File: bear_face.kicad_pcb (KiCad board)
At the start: 2 copper layers, 301.7 x 112.6 mm, 194 parts, among them J1 USB_B_Micro, J2 Conn_02x03_Odd_Even, Q1 2N7002, SW1 SW_Push, U1 ATmega32U4-AU, U2 SRV05-4, Y1 16MHz

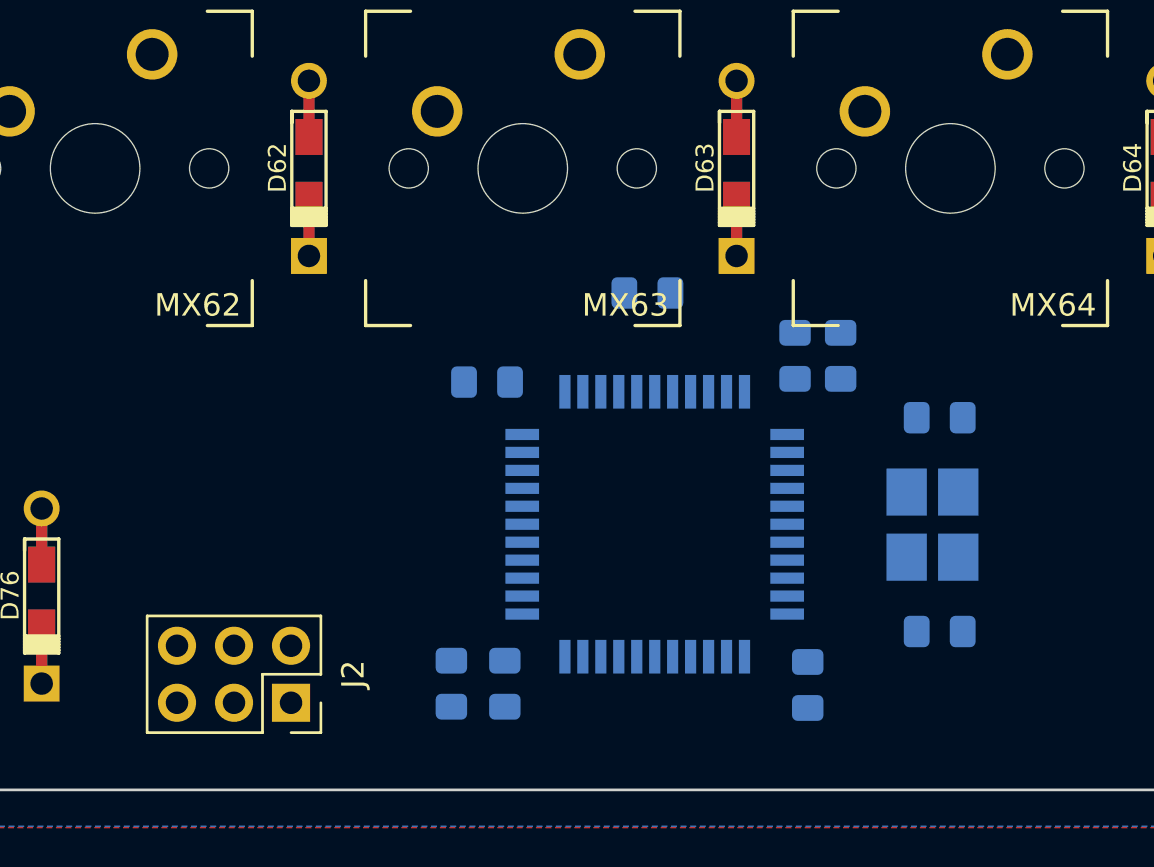
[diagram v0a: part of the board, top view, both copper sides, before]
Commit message: MCU components routed
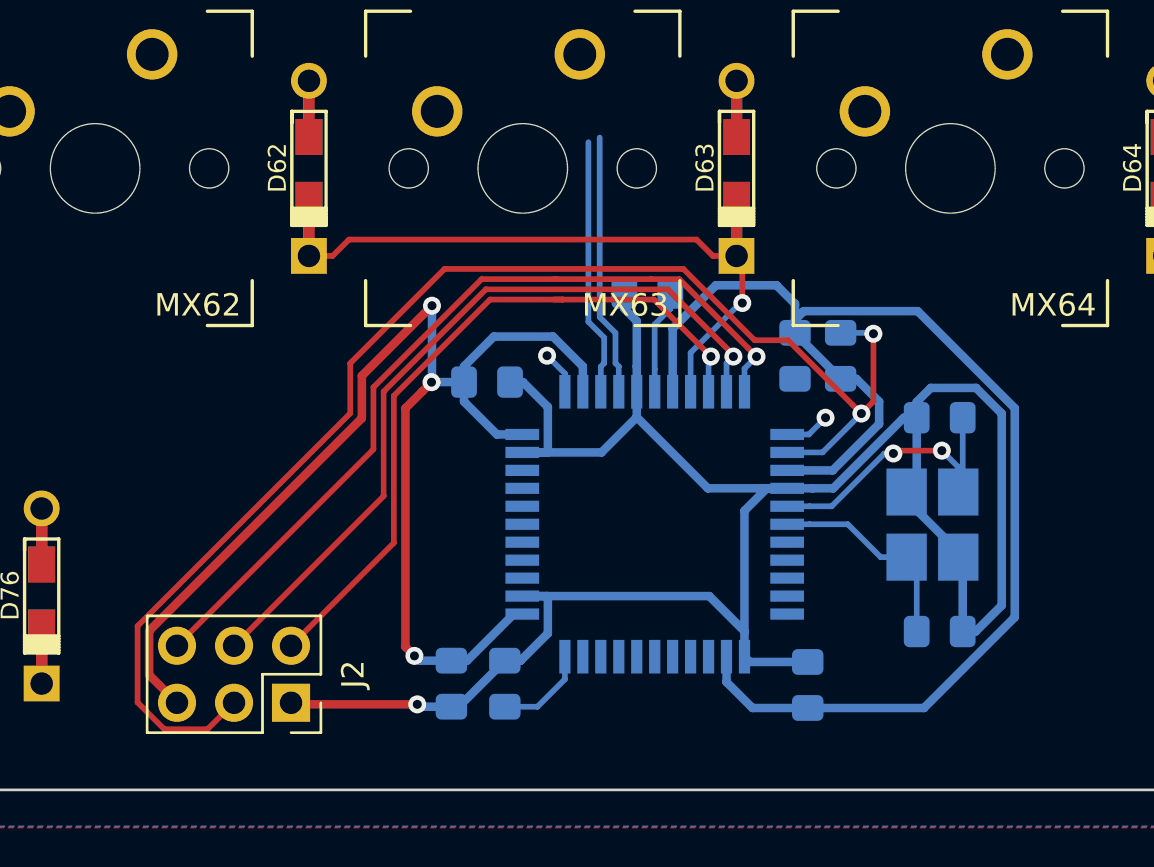
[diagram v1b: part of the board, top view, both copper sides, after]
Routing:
- net +5V: track 0.00 -> 118.6 mm, vias 0 -> 3
- net GND: track 0.00 -> 96.6 mm, vias 0 -> 1
- net RESET: track 0.00 -> 60.8 mm, vias 0 -> 2
- net MISO: track 0.00 -> 37.5 mm, vias 0 -> 1
- net MOSI: track 0.00 -> 34.5 mm, vias 0 -> 1
- net SCLK: track 0.00 -> 32.0 mm, vias 0 -> 1
- net ROW4: track 0.00 -> 26.8 mm, vias 0 -> 1
- net Net-(C2-Pad1): track 0.00 -> 13.5 mm, vias 0 -> 2
- net DB+: track 0.00 -> 11.7 mm
- net DB-: track 0.00 -> 11.5 mm
- net Net-(C1-Pad1): track 0.00 -> 9.43 mm
- net Net-(C3-Pad1): track 0.00 -> 4.69 mm
- net Net-(R87-Pad2): track 0.00 -> 4.19 mm
- net Net-(U1-Pad12): track 0.00 -> 2.02 mm, vias 0 -> 1
- net Net-(U1-Pad1): track 0.00 -> 1.94 mm, vias 0 -> 1

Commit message: Short switch-diode tracks routed
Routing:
- net Net-(D72-Pad2): track 0.00 -> 12.6 mm
- net Net-(D73-Pad2): track 0.00 -> 12.6 mm
- net Net-(D59-Pad2): track 0.00 -> 12.6 mm
- net Net-(D45-Pad2): track 0.00 -> 12.6 mm
- net Net-(D30-Pad2): track 0.00 -> 12.6 mm
- net Net-(D15-Pad2): track 0.00 -> 12.6 mm
- net Net-(D31-Pad2): track 0.00 -> 11.8 mm
- net Net-(D46-Pad2): track 0.00 -> 11.8 mm
- net Net-(D1-Pad2): track 0.00 -> 11.8 mm
- net Net-(D83-Pad2): track 0.00 -> 11.3 mm
- net Net-(D74-Pad2): track 0.00 -> 11.0 mm
- net Net-(D51-Pad2): track 0.00 -> 11.0 mm
- net Net-(D43-Pad2): track 0.00 -> 11.0 mm
- net Net-(D2-Pad2): track 0.00 -> 8.46 mm
- net Net-(D81-Pad2): track 0.00 -> 7.47 mm
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
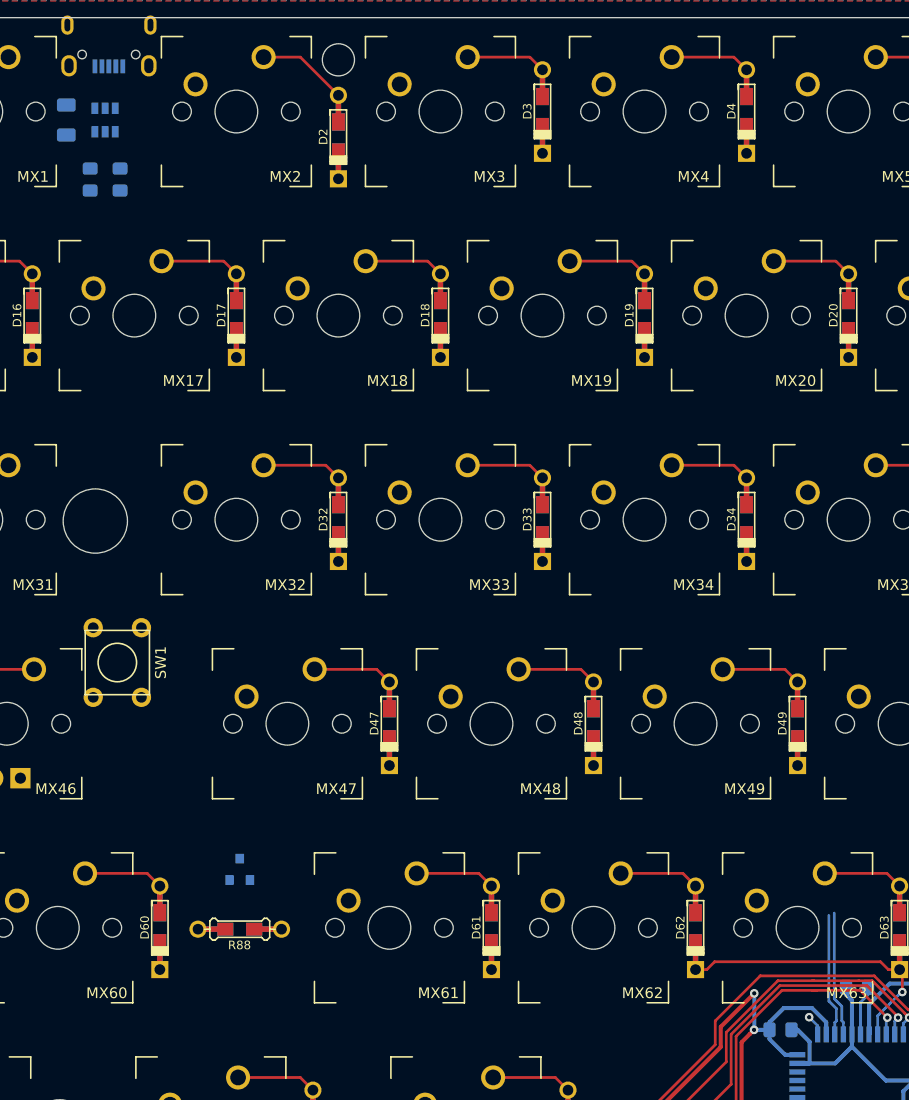
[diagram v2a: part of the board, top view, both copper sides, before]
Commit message: dPair routed
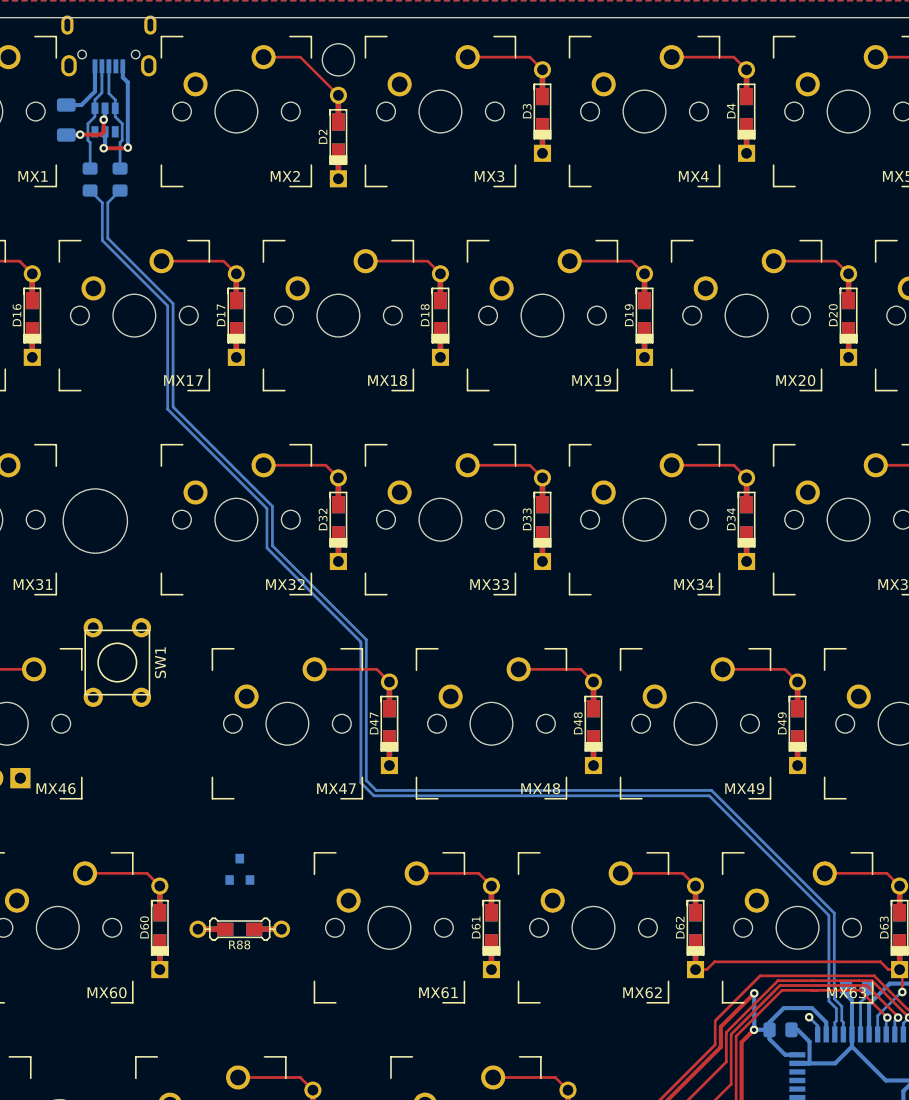
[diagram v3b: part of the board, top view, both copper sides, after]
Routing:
- net DB-: track 11.5 -> 126.0 mm
- net DB+: track 11.7 -> 126.0 mm
- net GND: track 96.6 -> 108.2 mm, vias 1 -> 3
- net DA-: track 0.00 -> 10.2 mm
- net DA+: track 0.00 -> 10.1 mm
- net +5V: track 118.6 -> 124.5 mm, vias 3 -> 5
- net VCC: track 0.00 -> 5.55 mm

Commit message: Rows routed
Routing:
- net ROW3: track 0.00 -> 319.0 mm
- net ROW2: track 0.00 -> 292.4 mm
- net ROW0: track 0.00 -> 288.7 mm
- net ROW1: track 0.00 -> 276.7 mm
- net ROW4: track 26.8 -> 271.4 mm
- net ROW5: track 0.00 -> 216.6 mm
- net GND: track 108.2 -> 126.1 mm

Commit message: Routing tweaks
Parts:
- added R5: R_Small, Keebio-Parts:Resistor-Hybrid, F.Cu at (77.0, 143.2)
- renumbered R85 to R1, R86 to R2, R87 to R3, R88 to R4
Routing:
- net COL1: track 0.00 -> 116.9 mm, vias 0 -> 1
- net COL2: track 0.00 -> 114.0 mm, vias 0 -> 1
- net COL0: track 0.00 -> 106.1 mm
- net COL3: track 0.00 -> 67.0 mm

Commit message: Columns routed, MCU pins broken out
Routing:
- net COL9: track 0.00 -> 112.9 mm
- net COL10: track 0.00 -> 112.9 mm
- net COL5: track 0.00 -> 111.0 mm
- net COL12: track 0.00 -> 108.0 mm
- net COL11: track 0.00 -> 108.0 mm
- net COL13: track 0.00 -> 107.9 mm
- net COL14: track 0.00 -> 101.0 mm
- net COL8: track 0.00 -> 90.9 mm
- net COL7: track 0.00 -> 90.9 mm
- net COL6: track 0.00 -> 90.9 mm
- net COL4: track 0.00 -> 90.9 mm
- net COL3: track 67.0 -> 90.9 mm, vias 0 -> 1
- net +5V: track 124.5 -> 142.1 mm, vias 5 -> 7
- net COL1: track 116.9 -> 130.1 mm
- net COL0: track 106.1 -> 118.5 mm
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
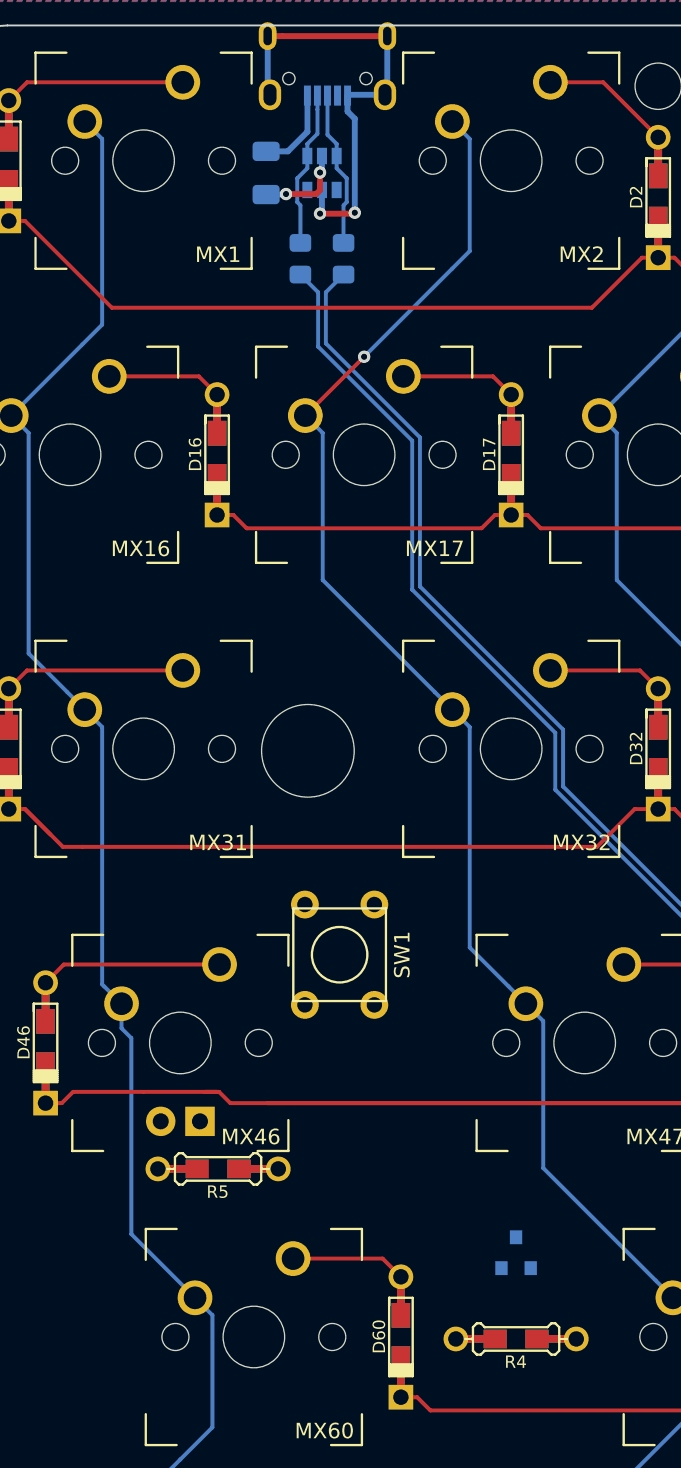
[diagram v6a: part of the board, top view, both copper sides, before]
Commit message: Updated ESD tracking, edited footprints
Caps key footprint LED pads now support xd75 hotswap LED sockets
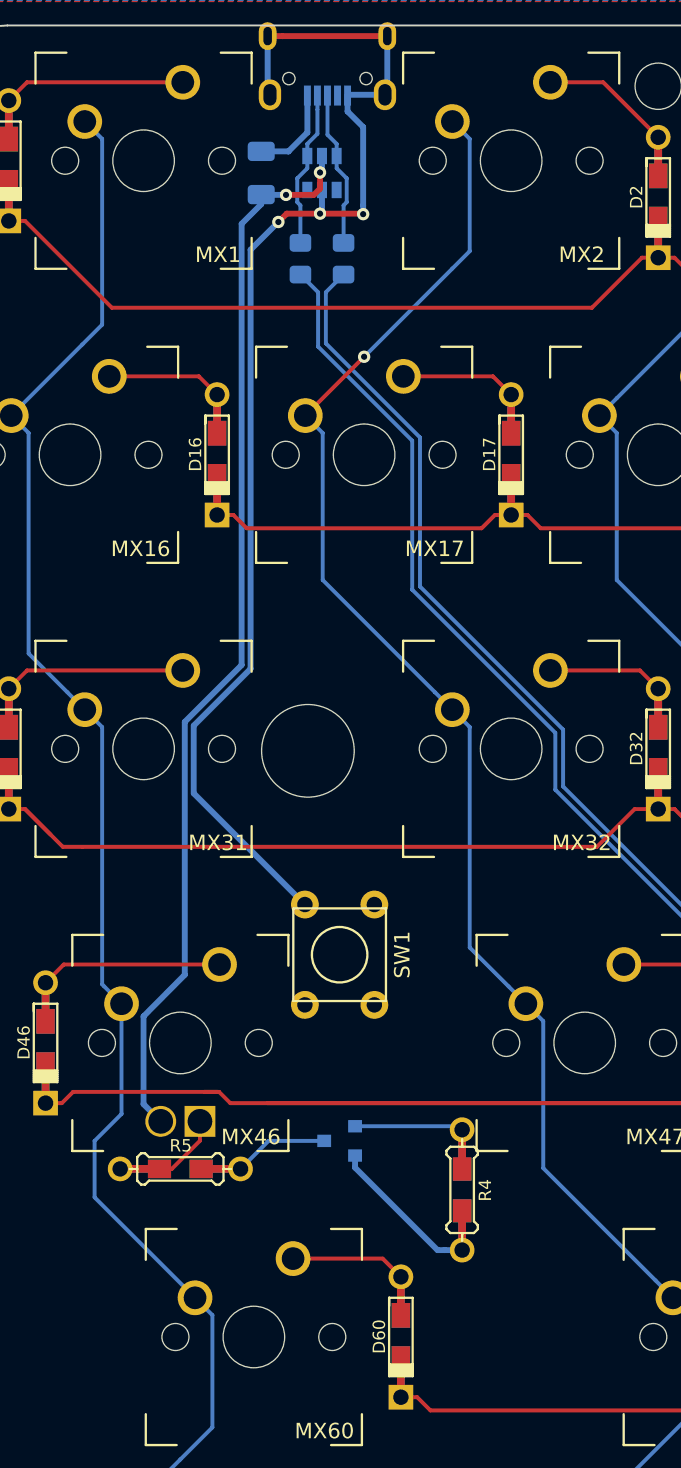
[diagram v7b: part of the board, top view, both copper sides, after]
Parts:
- MX46: footprint MX_Only:MXOnly-1.75U -> bear_face_parts:MXOnly-1.75U-CapsLED-XD75-socket
- moved Q1 13.5 mm to (84.9, 141.3), turned to 180 degrees
- moved R4 10.3 mm to (92.8, 144.5), turned to 90 degrees
- moved R5 2.45 mm to (74.6, 143.2), turned to 180 degrees
- moved F1 0.32 mm to (79.8, 78.6)
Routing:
- net +5V: track 142.1 -> 206.0 mm
- net GND: track 132.1 -> 195.2 mm, vias 3 -> 4
- net Net-(MX46-Pad4): track 0.00 -> 8.31 mm
- net LEDPIN: track 0.00 -> 7.03 mm
- net LEDOUT: track 0.00 -> 6.17 mm
- net COL0: track 118.5 -> 120.0 mm
